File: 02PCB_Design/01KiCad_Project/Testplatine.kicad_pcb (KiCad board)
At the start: 2 copper layers, 42.1 x 42.1 mm, 10 parts, among them J2 MTSW-104-22-L-D-265-RA, U1 ISM330BXTR, U2 AS5047P-ATSM

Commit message: Layout progress
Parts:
- added C10: 10uF, Capacitor_SMD:C_1210_3225Metric_Pad1.33x2.70mm_HandSolder, F.Cu at (66.4, 105.6)
- added C11: 10uF, Capacitor_SMD:C_1210_3225Metric_Pad1.33x2.70mm_HandSolder, F.Cu at (61.4, 105.6)
- added C12: 10uF, Capacitor_SMD:C_1210_3225Metric_Pad1.33x2.70mm_HandSolder, F.Cu at (56.4, 105.6)
- added C13: 10uF, Capacitor_SMD:C_1210_3225Metric_Pad1.33x2.70mm_HandSolder, F.Cu at (51.4, 105.6)
- added C14: 4.7uF, Capacitor_SMD:C_0805_2012Metric_Pad1.18x1.45mm_HandSolder, F.Cu at (70.6, 105.6)
- added C15: 4.7uF, Capacitor_SMD:C_0805_2012Metric_Pad1.18x1.45mm_HandSolder, F.Cu at (35.7, 133.6)
- added C16: 4.7uF, Capacitor_SMD:C_0805_2012Metric_Pad1.18x1.45mm_HandSolder, F.Cu at (31.1, 129.2)
- added C17: 33nF, Capacitor_SMD:C_0603_1608Metric_Pad1.08x0.95mm_HandSolder, F.Cu at (92.0, 110.0)
- added C18: 2.2uF, Capacitor_SMD:C_0805_2012Metric_Pad1.18x1.45mm_HandSolder, F.Cu at (81.3, 160.3)
- added C19: 0.1uF, Capacitor_SMD:C_0603_1608Metric_Pad1.08x0.95mm_HandSolder, F.Cu at (81.4, 162.2)
- added C20: 220nF, Capacitor_SMD:C_0805_2012Metric_Pad1.18x1.45mm_HandSolder, F.Cu at (90.2, 175.0)
- added C21: 220nF, Capacitor_SMD:C_0805_2012Metric_Pad1.18x1.45mm_HandSolder, F.Cu at (90.2, 172.8)
- added C22: 220nF, Capacitor_SMD:C_0805_2012Metric_Pad1.18x1.45mm_HandSolder, F.Cu at (90.2, 168.4)
- added C23: 1uF, Capacitor_SMD:C_0805_2012Metric_Pad1.18x1.45mm_HandSolder, F.Cu at (90.2, 170.6)
- added C24: 1uF, Capacitor_SMD:C_0805_2012Metric_Pad1.18x1.45mm_HandSolder, F.Cu at (86.3, 172.8)
- added C25: 1uF, Capacitor_SMD:C_0805_2012Metric_Pad1.18x1.45mm_HandSolder, F.Cu at (86.3, 175.0)
- added C26: 47p, Capacitor_SMD:C_0603_1608Metric_Pad1.08x0.95mm_HandSolder, F.Cu at (87.1, 164.3)
- added C27: 47p, Capacitor_SMD:C_0603_1608Metric_Pad1.08x0.95mm_HandSolder, F.Cu at (86.6, 162.7)
- added C28: 0.1uF, Capacitor_SMD:C_0603_1608Metric_Pad1.08x0.95mm_HandSolder, F.Cu at (90.0, 165.4)
- added C29: 0.1uF, Capacitor_SMD:C_0603_1608Metric_Pad1.08x0.95mm_HandSolder, F.Cu at (95.2, 165.4)
- added C30: 0.1uF, Capacitor_SMD:C_0603_1608Metric_Pad1.08x0.95mm_HandSolder, F.Cu at (157.0, 21.7)
- added C31: 33nF, Capacitor_SMD:C_0603_1608Metric_Pad1.08x0.95mm_HandSolder, F.Cu at (157.0, 24.2)
- added C32: 0.1uF, Capacitor_SMD:C_0603_1608Metric_Pad1.08x0.95mm_HandSolder, F.Cu at (157.0, 26.7)
- added C33: 2.2uF, Capacitor_SMD:C_0805_2012Metric_Pad1.18x1.45mm_HandSolder, F.Cu at (81.3, 138.6)
- added C34: 0.1uF, Capacitor_SMD:C_0603_1608Metric_Pad1.08x0.95mm_HandSolder, F.Cu at (81.4, 140.5)
- added C35: 220nF, Capacitor_SMD:C_0805_2012Metric_Pad1.18x1.45mm_HandSolder, F.Cu at (90.3, 153.3)
- added C36: 220nF, Capacitor_SMD:C_0805_2012Metric_Pad1.18x1.45mm_HandSolder, F.Cu at (90.3, 151.1)
- added C37: 220nF, Capacitor_SMD:C_0805_2012Metric_Pad1.18x1.45mm_HandSolder, F.Cu at (90.3, 148.9)
- added C38: 1uF, Capacitor_SMD:C_0805_2012Metric_Pad1.18x1.45mm_HandSolder, F.Cu at (90.3, 146.7)
- added C39: 1uF, Capacitor_SMD:C_0805_2012Metric_Pad1.18x1.45mm_HandSolder, F.Cu at (86.3, 153.3)
- added C4: 100nF, Capacitor_SMD:C_0603_1608Metric_Pad1.08x0.95mm_HandSolder, F.Cu at (97.8, 39.8)
- added C40: 1uF, Capacitor_SMD:C_0805_2012Metric_Pad1.18x1.45mm_HandSolder, F.Cu at (86.3, 151.1)
- added C41: 47p, Capacitor_SMD:C_0603_1608Metric_Pad1.08x0.95mm_HandSolder, F.Cu at (87.1, 142.6)
- added C42: 47p, Capacitor_SMD:C_0603_1608Metric_Pad1.08x0.95mm_HandSolder, F.Cu at (86.6, 141.0)
- added C43: 0.1uF, Capacitor_SMD:C_0603_1608Metric_Pad1.08x0.95mm_HandSolder, F.Cu at (90.0, 143.7)
- added C44: 0.1uF, Capacitor_SMD:C_0603_1608Metric_Pad1.08x0.95mm_HandSolder, F.Cu at (95.2, 143.7)
- added C45: 0.1uF, Capacitor_SMD:C_0603_1608Metric_Pad1.08x0.95mm_HandSolder, F.Cu at (180.1, 21.2)
- added C46: 33nF, Capacitor_SMD:C_0603_1608Metric_Pad1.08x0.95mm_HandSolder, F.Cu at (180.1, 23.7)
- added C47: 0.1uF, Capacitor_SMD:C_0603_1608Metric_Pad1.08x0.95mm_HandSolder, F.Cu at (180.1, 26.2)
- added C48: 2.2uF, Capacitor_SMD:C_0805_2012Metric_Pad1.18x1.45mm_HandSolder, F.Cu at (81.3, 117.3)
- added C49: 0.1uF, Capacitor_SMD:C_0603_1608Metric_Pad1.08x0.95mm_HandSolder, F.Cu at (81.4, 119.2)
- added C5: 10uF, Capacitor_SMD:C_1210_3225Metric_Pad1.33x2.70mm_HandSolder, F.Cu at (98.0, 30.6)
- added C50: 220nF, Capacitor_SMD:C_0805_2012Metric_Pad1.18x1.45mm_HandSolder, F.Cu at (90.3, 132.1)
- added C51: 220nF, Capacitor_SMD:C_0805_2012Metric_Pad1.18x1.45mm_HandSolder, F.Cu at (90.3, 129.9)
- added C52: 220nF, Capacitor_SMD:C_0805_2012Metric_Pad1.18x1.45mm_HandSolder, F.Cu at (90.3, 127.7)
- added C53: 1uF, Capacitor_SMD:C_0805_2012Metric_Pad1.18x1.45mm_HandSolder, F.Cu at (90.3, 125.5)
- added C54: 1uF, Capacitor_SMD:C_0805_2012Metric_Pad1.18x1.45mm_HandSolder, F.Cu at (86.3, 132.1)
- added C55: 1uF, Capacitor_SMD:C_0805_2012Metric_Pad1.18x1.45mm_HandSolder, F.Cu at (86.3, 129.9)
- added C56: 47p, Capacitor_SMD:C_0603_1608Metric_Pad1.08x0.95mm_HandSolder, F.Cu at (87.1, 121.4)
- added C57: 47p, Capacitor_SMD:C_0603_1608Metric_Pad1.08x0.95mm_HandSolder, F.Cu at (86.6, 119.8)
- added C58: 0.1uF, Capacitor_SMD:C_0603_1608Metric_Pad1.08x0.95mm_HandSolder, F.Cu at (90.0, 122.5)
- added C59: 0.1uF, Capacitor_SMD:C_0603_1608Metric_Pad1.08x0.95mm_HandSolder, F.Cu at (95.2, 122.5)
- added C6: 1uF, Capacitor_SMD:C_0603_1608Metric_Pad1.08x0.95mm_HandSolder, F.Cu at (100.6, 35.6)
- added C60: 0.1uF, Capacitor_SMD:C_0603_1608Metric_Pad1.08x0.95mm_HandSolder, F.Cu at (202.0, 20.3)
- added C61: 33nF, Capacitor_SMD:C_0603_1608Metric_Pad1.08x0.95mm_HandSolder, F.Cu at (202.0, 22.8)
- added C62: 0.1uF, Capacitor_SMD:C_0603_1608Metric_Pad1.08x0.95mm_HandSolder, F.Cu at (202.0, 25.3)
- added C63: 2.2nF, Capacitor_SMD:C_0603_1608Metric_Pad1.08x0.95mm_HandSolder, F.Cu at (111.6, 158.2)
- added C64: 2.2nF, Capacitor_SMD:C_0603_1608Metric_Pad1.08x0.95mm_HandSolder, F.Cu at (98.4, 97.5)
- added C65: 2.2nF, Capacitor_SMD:C_0603_1608Metric_Pad1.08x0.95mm_HandSolder, F.Cu at (102.7, 97.5)
- added C66: 2.2nF, Capacitor_SMD:C_0603_1608Metric_Pad1.08x0.95mm_HandSolder, F.Cu at (112.9, 97.5)
- added C67: 2.2nF, Capacitor_SMD:C_0603_1608Metric_Pad1.08x0.95mm_HandSolder, F.Cu at (108.6, 97.5)
- added C68: 2.2nF, Capacitor_SMD:C_0603_1608Metric_Pad1.08x0.95mm_HandSolder, F.Cu at (130.4, 148.6)
- added C69: 2.2nF, Capacitor_SMD:C_0603_1608Metric_Pad1.08x0.95mm_HandSolder, F.Cu at (126.6, 148.6)
- added C7: 47uF, Capacitor_THT:CP_Radial_D8.0mm_P3.50mm, F.Cu at (99.2, 48.9)
- added C70: 0.1uF, Capacitor_SMD:C_0603_1608Metric_Pad1.08x0.95mm_HandSolder, F.Cu at (147.0, 167.5)
- added C71: 0.1uF, Capacitor_SMD:C_0603_1608Metric_Pad1.08x0.95mm_HandSolder, F.Cu at (153.2, 171.1)
- added C8: 470uF, Capacitor_THT:CP_Radial_D16.0mm_P7.50mm, F.Cu at (79.5, 95.0)
- added C9: 470uF, Capacitor_THT:CP_Radial_D16.0mm_P7.50mm, F.Cu at (41.9, 94.7)
- added J1: MTSW-104-22-L-D-265-RA, Connector_PinHeader_2.54mm:PinHeader_2x04_P2.54mm_Horizontal, F.Cu at (271.8, 15.2)
- added J3: FCR7350R, Connector:Banana_Jack_1Pin, F.Cu at (61.0, 95.7)
- added J4: FCR7350R, Connector:Banana_Jack_1Pin, F.Cu at (30.4, 95.7)
- added J5: DE9_Receptacle_MountingHoles, Connector_Dsub:DSUB-9_Female_Horizontal_P2.77x2.84mm_EdgePinOffset4.94mm_Housed_MountingHolesOffset7.48mm, F.Cu at (151.6, 179.4)
- added J6: MTSW-104-22-L-D-265-RA, Connector_PinHeader_2.54mm:PinHeader_2x04_P2.54mm_Horizontal, F.Cu at (106.8, 179.3)
- added J7: Conn_01x06_Pin, Connector_PinHeader_2.54mm:PinHeader_2x03_P2.54mm_Horizontal, F.Cu at (121.5, 179.3)
- added L1: 22uH, Inductor_SMD:L_Wuerth_MAPI-4020, F.Cu at (97.8, 43.0)
- added R1: 100k, Resistor_SMD:R_0603_1608Metric_Pad0.98x0.95mm_HandSolder, F.Cu at (271.6, 31.4)
- added R10: 20, Resistor_SMD:R_0603_1608Metric_Pad0.98x0.95mm_HandSolder, F.Cu at (87.4, 160.1)
- added R11: 20, Resistor_SMD:R_0603_1608Metric_Pad0.98x0.95mm_HandSolder, F.Cu at (85.7, 160.1)
- added R12: 3R, Resistor_SMD:R_0603_1608Metric_Pad0.98x0.95mm_HandSolder, F.Cu at (92.6, 166.4)
- added R13: 3.3m, Resistor_SMD:R_2512_6332Metric_Pad1.40x3.35mm_HandSolder, F.Cu at (75.7, 169.9)
- added R14: 100k, Resistor_SMD:R_0603_1608Metric_Pad0.98x0.95mm_HandSolder, F.Cu at (161.3, 26.7)
- added R15: 4.22k, Resistor_SMD:R_0603_1608Metric_Pad0.98x0.95mm_HandSolder, F.Cu at (161.3, 29.2)
- added R16: 3R, Resistor_SMD:R_0603_1608Metric_Pad0.98x0.95mm_HandSolder, F.Cu at (84.1, 141.4)
- added R17: 20, Resistor_SMD:R_0603_1608Metric_Pad0.98x0.95mm_HandSolder, F.Cu at (87.4, 138.4)
- added R18: 20, Resistor_SMD:R_0603_1608Metric_Pad0.98x0.95mm_HandSolder, F.Cu at (85.7, 138.4)
- added R19: 3R, Resistor_SMD:R_0603_1608Metric_Pad0.98x0.95mm_HandSolder, F.Cu at (92.6, 144.7)
- added R2: 33R, Resistor_SMD:R_0603_1608Metric_Pad0.98x0.95mm_HandSolder, F.Cu at (271.6, 34.0)
- added R20: 3.3m, Resistor_SMD:R_2512_6332Metric_Pad1.40x3.35mm_HandSolder, F.Cu at (75.4, 148.1)
- added R21: 100k, Resistor_SMD:R_0603_1608Metric_Pad0.98x0.95mm_HandSolder, F.Cu at (184.5, 26.2)
- added R22: 4.22k, Resistor_SMD:R_0603_1608Metric_Pad0.98x0.95mm_HandSolder, F.Cu at (184.5, 28.7)
- added R23: 3R, Resistor_SMD:R_0603_1608Metric_Pad0.98x0.95mm_HandSolder, F.Cu at (84.1, 120.2)
- added R24: 20, Resistor_SMD:R_0603_1608Metric_Pad0.98x0.95mm_HandSolder, F.Cu at (87.4, 117.2)
- added R25: 20, Resistor_SMD:R_0603_1608Metric_Pad0.98x0.95mm_HandSolder, F.Cu at (85.7, 117.2)
- added R26: 3R, Resistor_SMD:R_0603_1608Metric_Pad0.98x0.95mm_HandSolder, F.Cu at (92.6, 123.4)
- added R27: 3.3m, Resistor_SMD:R_2512_6332Metric_Pad1.40x3.35mm_HandSolder, F.Cu at (75.2, 127.3)
- added R28: 100k, Resistor_SMD:R_0603_1608Metric_Pad0.98x0.95mm_HandSolder, F.Cu at (206.3, 25.3)
- added R29: 4.22k, Resistor_SMD:R_0603_1608Metric_Pad0.98x0.95mm_HandSolder, F.Cu at (206.3, 27.9)
- added R3: 100k, Resistor_SMD:R_0603_1608Metric_Pad0.98x0.95mm_HandSolder, F.Cu at (271.6, 36.5)
- added R30: 33R, Resistor_SMD:R_0603_1608Metric_Pad0.98x0.95mm_HandSolder, F.Cu at (108.8, 159.2)
- added R31: 20R, Resistor_SMD:R_0603_1608Metric_Pad0.98x0.95mm_HandSolder, F.Cu at (112.4, 161.0)
- added R32: 33R, Resistor_SMD:R_0603_1608Metric_Pad0.98x0.95mm_HandSolder, F.Cu at (114.2, 159.2)
- added R33: 20R, Resistor_SMD:R_0603_1608Metric_Pad0.98x0.95mm_HandSolder, F.Cu at (112.1, 100.1)
- added R34: 20R, Resistor_SMD:R_0603_1608Metric_Pad0.98x0.95mm_HandSolder, F.Cu at (109.6, 100.3)
- added R35: 20R, Resistor_SMD:R_0603_1608Metric_Pad0.98x0.95mm_HandSolder, F.Cu at (99.4, 100.1)
- added R36: 20R, Resistor_SMD:R_0603_1608Metric_Pad0.98x0.95mm_HandSolder, F.Cu at (101.7, 100.1)
- added R37: 20R, Resistor_SMD:R_0603_1608Metric_Pad0.98x0.95mm_HandSolder, F.Cu at (129.4, 145.8)
- added R38: 20R, Resistor_SMD:R_0603_1608Metric_Pad0.98x0.95mm_HandSolder, F.Cu at (127.3, 145.8)
- added R39: 33R, Resistor_SMD:R_0603_1608Metric_Pad0.98x0.95mm_HandSolder, B.Cu at (142.2, 157.8)
- added R4: 33R, Resistor_SMD:R_0603_1608Metric_Pad0.98x0.95mm_HandSolder, F.Cu at (271.6, 39.0)
- added R40: 33R, Resistor_SMD:R_0603_1608Metric_Pad0.98x0.95mm_HandSolder, B.Cu at (120.8, 158.0)
- added R41: 33R, Resistor_SMD:R_0603_1608Metric_Pad0.98x0.95mm_HandSolder, B.Cu at (125.8, 158.0)
- added R42: 0R, Resistor_SMD:R_0603_1608Metric_Pad0.98x0.95mm_HandSolder, F.Cu at (151.8, 161.3)
- added R45: 0R, Resistor_SMD:R_0603_1608Metric_Pad0.98x0.95mm_HandSolder, F.Cu at (149.8, 161.3)
- added R46: 120, Resistor_SMD:R_0603_1608Metric_Pad0.98x0.95mm_HandSolder, F.Cu at (148.1, 175.0)
- added R7: 100k, Resistor_SMD:R_0603_1608Metric_Pad0.98x0.95mm_HandSolder, F.Cu at (90.4, 106.6)
- added R8: 4.22k, Resistor_SMD:R_0603_1608Metric_Pad0.98x0.95mm_HandSolder, F.Cu at (90.4, 110.0)
- added R9: 3R, Resistor_SMD:R_0603_1608Metric_Pad0.98x0.95mm_HandSolder, F.Cu at (84.1, 163.1)
- added U10: INA240A1PW, Package_SO:TSSOP-8_4.4x3mm_P0.65mm, F.Cu at (74.8, 121.2)
- added U11: NUCLEO-G431RB, footprints:NucleoMorphoG431RB, F.Cu at (124.5, 121.7)
- added U12: MCP2562FD, Package_SO:SOIC-8_3.9x4.9mm_P1.27mm, F.Cu at (148.6, 171.1)
- added U3: L6982, Package_SO:TSSOP-8_3x3mm_P0.65mm, F.Cu at (98.0, 35.6)
- added U4: AP2114D, Package_TO_SOT_SMD:TO-252-2, F.Cu at (35.8, 126.2)
- added U5: LMG2100R044RARR, footprints:RAR0016B-MFG, F.Cu at (85.0, 168.4)
- added U6: INA240A1PW, Package_SO:TSSOP-8_4.4x3mm_P0.65mm, F.Cu at (75.6, 163.8)
- added U7: LMG2100R044RARR, footprints:RAR0016B-MFG, F.Cu at (85.0, 146.8)
- added U8: INA240A1PW, Package_SO:TSSOP-8_4.4x3mm_P0.65mm, F.Cu at (75.0, 142.0)
- added U9: LMG2100R044RARR, footprints:RAR0016B-MFG, F.Cu at (85.1, 125.6)
- C1: footprint Capacitor_SMD:C_0402_1005Metric_Pad0.74x0.62mm_HandSolder -> Package_SO:SOIC-8_3.9x4.9mm_P1.27mm
- C2, C3: footprint Capacitor_SMD:C_0402_1005Metric_Pad0.74x0.62mm_HandSolder -> Capacitor_SMD:C_0603_1608Metric_Pad1.08x0.95mm_HandSolder
- J2: value MTSW-104-22-L-D-265-RA -> Screw_Terminal_01x03; footprint MyFootprintLib:SAMTEC_MTSW-104-22-L-D-265-RA -> TerminalBlock_Phoenix:TerminalBlock_Phoenix_MKDS-3-3-5.08_1x03_P5.08mm_Horizontal
- U1: value ISM330BXTR -> AS5047P-ATSM; footprint MyFootprintLib:XDCR_ISM330BXTR -> Package_SO:TSSOP-14_4.4x5mm_P0.65mm
- U2: value AS5047P-ATSM -> ISM330BXTR; footprint MyFootprintLib:SOP65P640X120-14N -> Package_LGA:LGA-14_3x2.5mm_P0.5mm_LayoutBorder3x4y; moved to F.Cu
- moved H4 200.1 mm to (275.0, 144.9)
- moved H1 187.6 mm to (275.0, 130.0)
- moved H2 182.7 mm to (275.0, 140.2)
- moved C3 182.7 mm to (271.6, 28.9), turned to 0 degrees
- moved H3 179.1 mm to (275.0, 150.3)
- moved U1 176.9 mm to (278.2, 28.5), turned to 0 degrees
- moved U2 174.8 mm to (271.8, 42.3), turned to 0 degrees
- moved C1 174.1 mm to (278.0, 35.1), turned to 0 degrees
- moved C2 168.2 mm to (271.6, 26.4)
- moved J2 101.4 mm to (26.5, 143.3), turned to -90 degrees
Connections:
- C1 pad 1: /SensorSheet/3.3SPI -> +3.3VP
- C1 pad 2: GND -> GND1
- C2 pad 1: /SensorSheet/3.3SPI -> +3.3VP
- C2 pad 2: GND -> GND1
- C3 pad 1: /SensorSheet/3.3SPI -> +3.3VP
- C3 pad 2: GND -> GND1
- U1 pad 1: /SensorSheet/SPI_MISO -> /SensorSheet/ENC_CS
- U1 pad 11: /SensorSheet/3.3SPI -> +3.3VP
- U1 pad 12: /SensorSheet/IMU_CS -> +3.3VP
- U1 pad 13: /SensorSheet/SPI_SCLK -> GND1
- U1 pad 14: /SensorSheet/SPI_MOSI -> unconnected-(U1-I/PWM-Pad14)
- U1 pad 2: /SensorSheet/3.3SPI -> /SensorSheet/SPI_SCLK
- U1 pad 3: /SensorSheet/3.3SPI -> Net-(U1-MISO)
- U1 pad 4: /SensorSheet/IMU_INT1 -> /SensorSheet/SPI_MOSI
- U1 pad 5: /SensorSheet/3.3SPI -> GND1
- U1 pad 6: /SensorSheet/3.3SPI -> unconnected-(U1-B-Pad6)
- U1 pad 7: GND -> unconnected-(U1-A-Pad7)
- U1 pad 8: /SensorSheet/3.3SPI -> unconnected-(U1-W/PWM-Pad8)
- U1 pad 9: /SensorSheet/3.3SPI -> unconnected-(U1-V-Pad9)
- U2 pad 1: /SensorSheet/ENC_CS -> Net-(U2-SDO/TA0)
- U2 pad 11: /SensorSheet/3.3SPI -> +3.3VP
- U2 pad 12: /SensorSheet/3.3SPI -> /SensorSheet/IMU_CS
- U2 pad 13: GND -> /SensorSheet/SPI_SCLK
- U2 pad 14: unconnected-(U2-I/PWM-Pad14) -> /SensorSheet/SPI_MOSI
- U2 pad 2: /SensorSheet/SPI_SCLK -> +3.3VP
- U2 pad 3: /SensorSheet/SPI_MISO -> +3.3VP
- U2 pad 4: /SensorSheet/SPI_MOSI -> /SensorSheet/IMU_INT1
- U2 pad 5: GND -> +3.3VP
- U2 pad 6: unconnected-(U2-B-Pad6) -> +3.3VP
- U2 pad 7: unconnected-(U2-A-Pad7) -> GND1
- U2 pad 8: unconnected-(U2-W/PWM-Pad8) -> +3.3VP
- U2 pad 9: unconnected-(U2-V-Pad9) -> +3.3VP
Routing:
- net /SensorSheet/3.3SPI: track 77.4 -> 0.00 mm, vias 1 -> 0
- net /SensorSheet/SPI_MOSI: track 24.8 -> 0.00 mm, vias 1 -> 0
- net /SensorSheet/IMU_INT1: track 23.3 -> 0.00 mm
- net /SensorSheet/SPI_MISO: track 19.6 -> 0.00 mm, vias 1 -> 0
- net /SensorSheet/SPI_SCLK: track 19.1 -> 0.00 mm, vias 1 -> 0
- net /SensorSheet/ENC_CS: track 15.6 -> 0.00 mm
- net /SensorSheet/IMU_CS: track 14.9 -> 0.00 mm
- net GND: track 4.01 -> 0.00 mm, vias 4 -> 0
- added copper zone on F.Cu, net +24V
- added copper zone on F.Cu, net GNDPWR
- removed copper zone on B.Cu, net GND
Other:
- board size 42.1 x 42.1 mm -> 146 x 100 mm
- copper layers 2 -> 4
- board text removed: "locked"

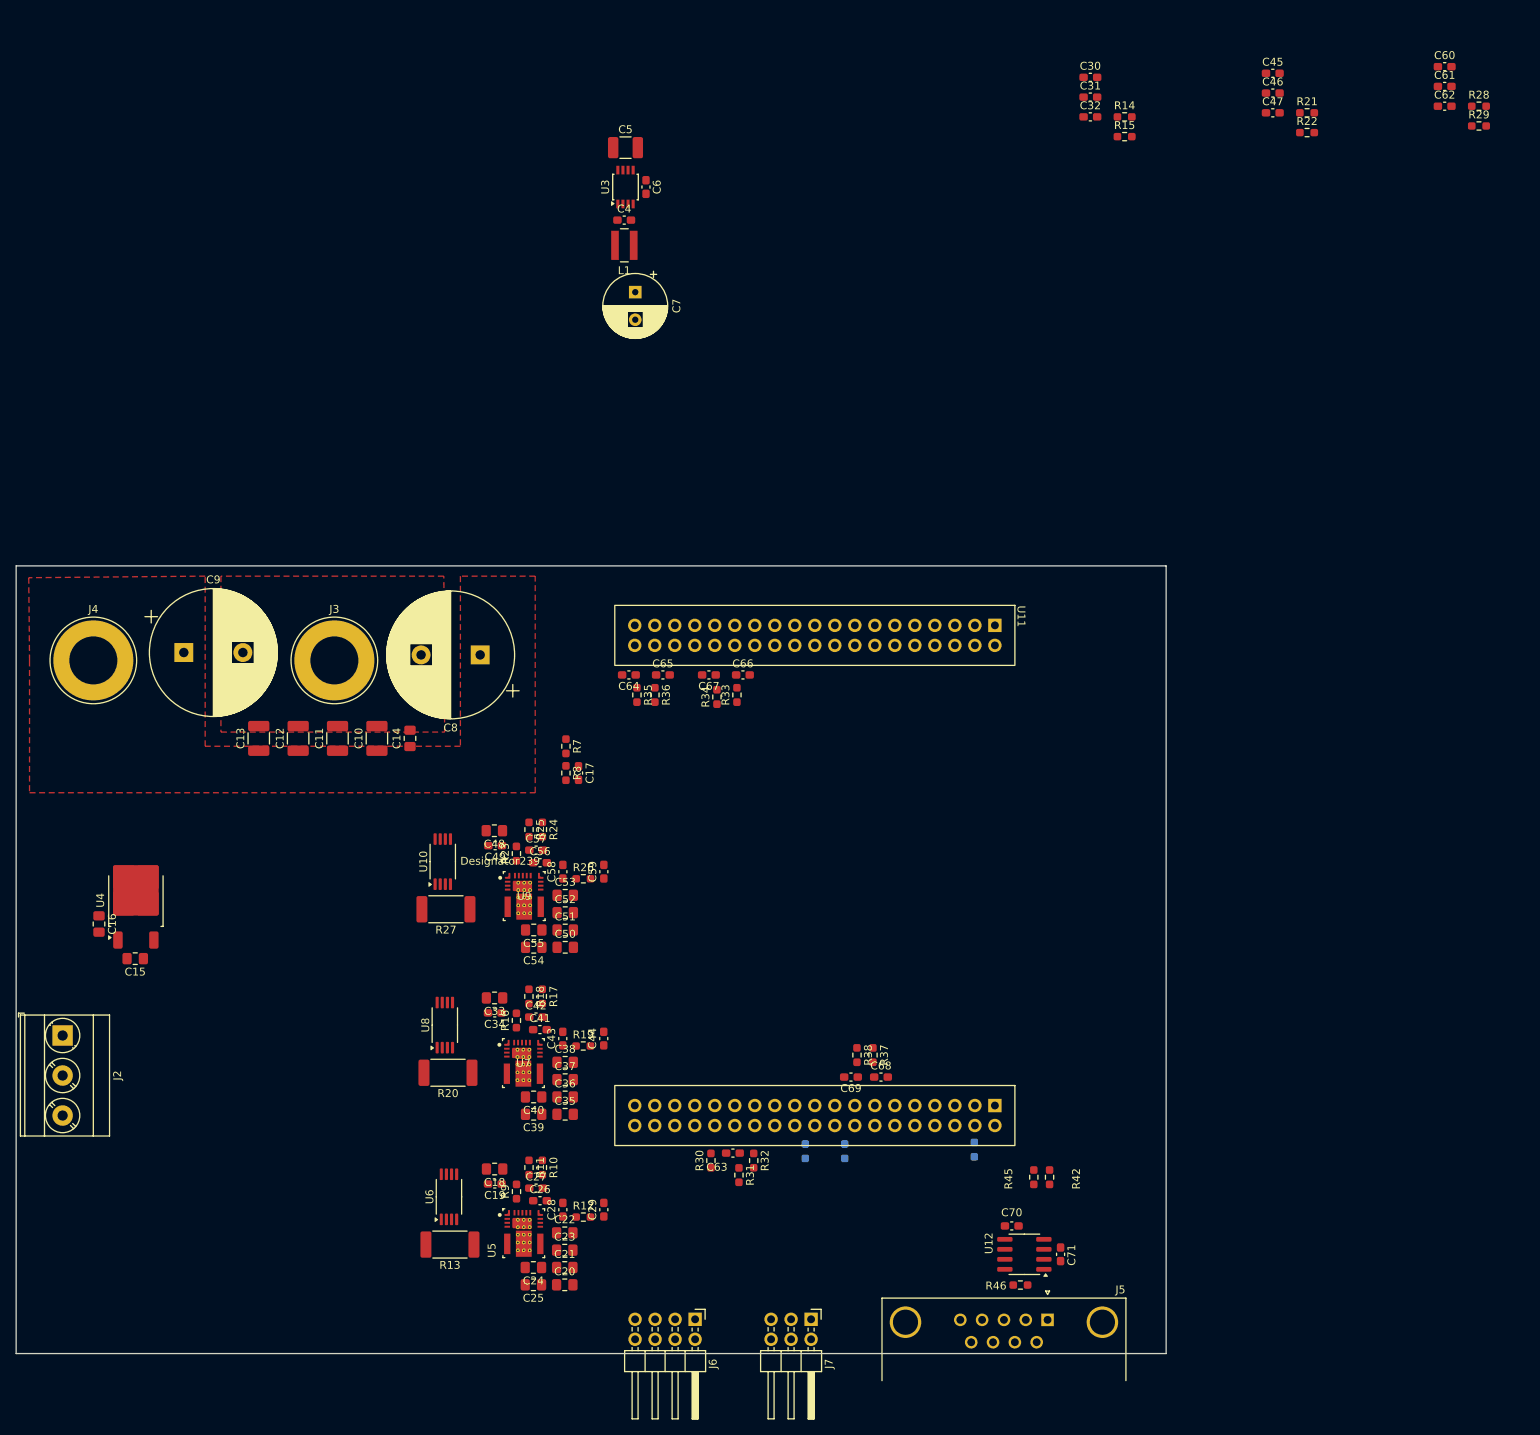
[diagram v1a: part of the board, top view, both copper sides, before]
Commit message: routed signals
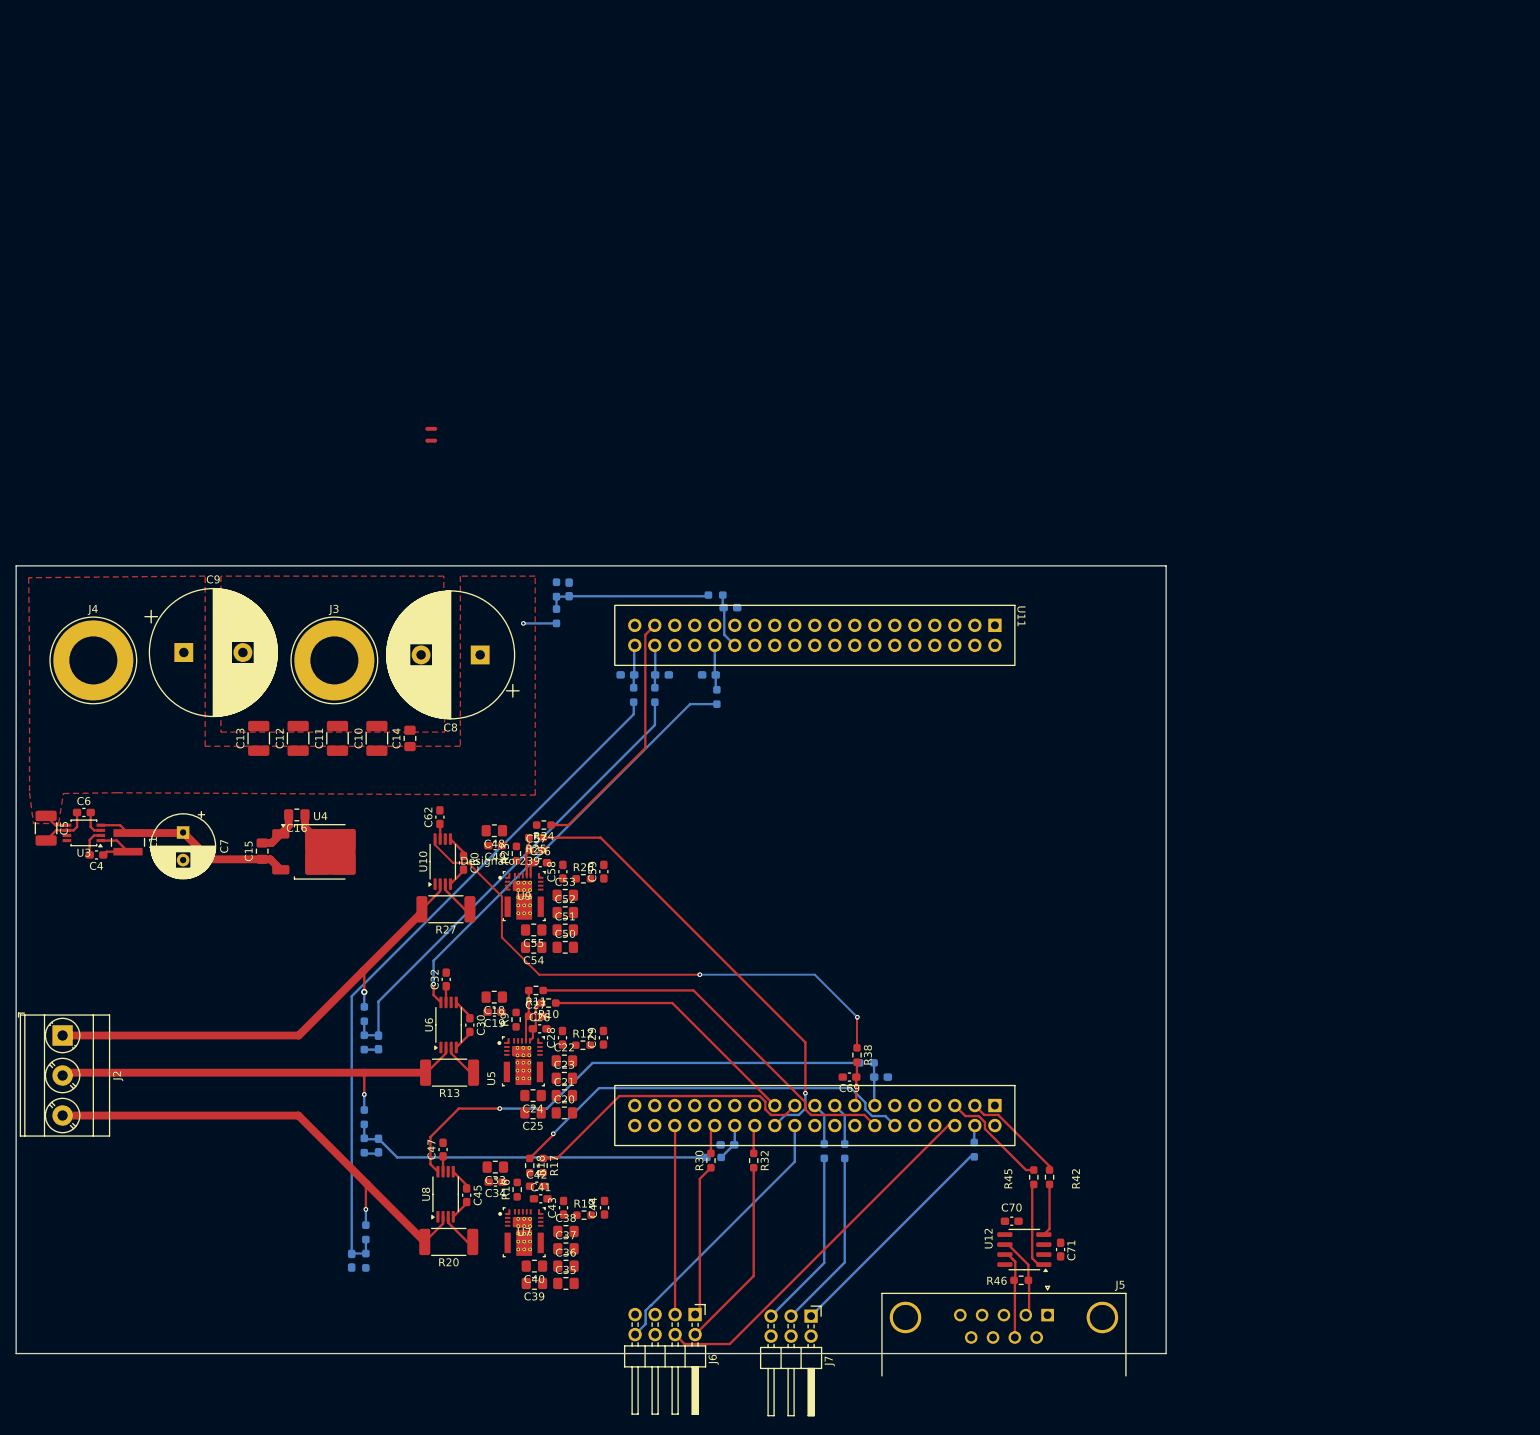
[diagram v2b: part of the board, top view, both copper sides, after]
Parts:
- added NT1: NetTie_2, NetTie:NetTie-2_SMD_Pad0.5mm, F.Cu at (73.3, 66.3)
- added NT2: NetTie_2, NetTie:NetTie-2_SMD_Pad0.5mm, F.Cu at (73.3, 67.8)
- C17, C31, C46, C61, C63, C64, C65, C66, C67, C68, R14, R15, R21, R22, R28, R29, R31, R33, R34, R35, R36, R37, R7, R8: moved to B.Cu
- moved C46 188.8 mm to (63.2, 171.9), turned to -90 degrees
- moved R22 186.5 mm to (65.0, 171.9), turned to -90 degrees
- moved R21 185.7 mm to (65.0, 168.3), turned to -90 degrees
- moved R29 183.2 mm to (64.8, 144.2), turned to -90 degrees
- moved R28 182.5 mm to (64.8, 140.6), turned to -90 degrees
- moved C61 181.8 mm to (66.6, 144.2), turned to -90 degrees
- moved C45 175.4 mm to (77.8, 163.6), turned to -90 degrees
- moved C47 168.6 mm to (74.8, 157.8), turned to 90 degrees
- moved C31 160.9 mm to (66.6, 157.3), turned to -90 degrees
- moved C60 160.4 mm to (77.4, 121.4), turned to -90 degrees
- moved R15 160.4 mm to (64.8, 157.3), turned to -90 degrees
- moved R14 159.5 mm to (64.8, 153.7), turned to -90 degrees
- moved C62 156.3 mm to (74.4, 115.6), turned to 90 degrees
- moved C30 143.8 mm to (78.2, 142.0), turned to -90 degrees
- moved C32 136.7 mm to (75.2, 136.2), turned to 90 degrees
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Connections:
- J2 pad 2: /escSheet/HalfBridgePowerStage2/PH_OUT -> /escSheet/HalfBridgePowerStage1/PH_OUT
- J2 pad 3: /escSheet/HalfBridgePowerStage1/PH_OUT -> /escSheet/HalfBridgePowerStage2/PH_OUT
- J5 pad 9: unconnected-(J5-Pad9) -> +5V
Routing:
- net /escSheet/HalfBridgePowerStage2/V_PHASE: track 0.00 -> 88.4 mm
- net /escSheet/HalfBridgePowerStage3/I_PHASE: track 0.00 -> 70.4 mm, vias 0 -> 2
- net /escSheet/HalfBridgePowerStage2/I_PHASE: track 0.00 -> 63.2 mm, vias 0 -> 1
- net /escSheet/HalfBridgePowerStage2/PH_OUT: track 0.00 -> 62.1 mm, vias 0 -> 1
- net /escSheet/HalfBridgePowerStage3/PH_OUT: track 0.00 -> 60.9 mm, vias 0 -> 1
- net /escSheet/HalfBridgePowerStage3/V_PHASE: track 0.00 -> 60.4 mm
- net /escSheet/HalfBridgePowerStage3/PWM_LI: track 0.00 -> 57.2 mm, vias 0 -> 1
- net /escSheet/HalfBridgePowerStage1/I_PHASE: track 0.00 -> 55.1 mm, vias 0 -> 1
- net /escSheet/HalfBridgePowerStage1/PH_OUT: track 0.00 -> 54.7 mm, vias 0 -> 1
- net /escSheet/HalfBridgePowerStage2/PWM_LI: track 0.00 -> 52.6 mm, vias 0 -> 1
- net /escSheet/HalfBridgePowerStage1/PWM_LI: track 0.00 -> 49.7 mm
- net /escSheet/Bus_Connectors/IMU_CS: track 0.00 -> 47.5 mm
- net /escSheet/HalfBridgePowerStage1/V_PHASE: track 0.00 -> 46.2 mm
- net /escSheet/HalfBridgePowerStage2/PWM_HI: track 0.00 -> 37.1 mm
- net /escSheet/Bus_Connectors/IMU_INT1: track 0.00 -> 35.0 mm
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
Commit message: Design 1.0 Finished
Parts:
- removed NT1, NT2: NetTie_2, NetTie:NetTie-2_SMD_Pad0.5mm
- C1: footprint Package_SO:SOIC-8_3.9x4.9mm_P1.27mm -> Capacitor_SMD:C_0603_1608Metric_Pad1.08x0.95mm_HandSolder; moved to B.Cu
- R1, R2, U1: moved to B.Cu
- moved J1 88.0 mm to (220.3, 86.6), turned to 135 degrees
- moved U1 79.6 mm to (233.2, 94.1), turned to -135 degrees
- moved C1 78.7 mm to (229.2, 96.9), turned to 135 degrees
- moved C5 74.7 mm to (83.0, 70.7), turned to 180 degrees
- moved H4 74.4 mm to (220.7, 94.1)
- moved R2 71.6 mm to (229.1, 91.5), turned to -45 degrees
- moved R1 71.2 mm to (229.2, 88.7), turned to -45 degrees
- moved C2 68.6 mm to (241.6, 88.2), turned to 90 degrees
- moved C6 68.4 mm to (85.0, 75.5), turned to 90 degrees
- moved U3 67.9 mm to (82.5, 75.5), turned to 90 degrees
- moved C4 65.3 mm to (79.7, 77.1), turned to 90 degrees
- moved C3 64.4 mm to (240.6, 85.4)
- moved R3 64.0 mm to (234.4, 88.5), turned to 180 degrees
- moved H1 63.9 mm to (233.2, 81.6)
- moved H3 63.3 mm to (245.7, 94.1)
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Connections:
- C10 pad 2: GNDPWR -> GNDA
- C11 pad 2: GNDPWR -> GNDA
- C12 pad 2: GNDPWR -> GNDA
- C13 pad 2: GNDPWR -> GNDA
- C14 pad 2: GNDPWR -> GNDA
- C20 pad 2: GNDPWR -> GNDA
- C21 pad 2: GNDPWR -> GNDA
- C22 pad 2: GNDPWR -> GNDA
- C23 pad 2: GNDPWR -> GNDA
- C24 pad 2: GNDPWR -> GNDA
- C25 pad 2: GNDPWR -> GNDA
- C35 pad 2: GNDPWR -> GNDA
- C36 pad 2: GNDPWR -> GNDA
- C37 pad 2: GNDPWR -> GNDA
- C38 pad 2: GNDPWR -> GNDA
- C39 pad 2: GNDPWR -> GNDA
- C40 pad 2: GNDPWR -> GNDA
- C50 pad 2: GNDPWR -> GNDA
- C51 pad 2: GNDPWR -> GNDA
- C52 pad 2: GNDPWR -> GNDA
- C53 pad 2: GNDPWR -> GNDA
- C54 pad 2: GNDPWR -> GNDA
- C55 pad 2: GNDPWR -> GNDA
- C7 pad 2: GNDPWR -> GNDA
- C8 pad 2: GNDPWR -> GNDA
- C9 pad 2: GNDPWR -> GNDA
- J1 pad 1: (no net) -> /SensorSheet/IMU_INT1
- J1 pad 2: (no net) -> /SensorSheet/SPI_MOSI
- J1 pad 3: (no net) -> /SensorSheet/SPI_MISO
- J1 pad 4: (no net) -> +3.3VP
- J1 pad 5: (no net) -> /SensorSheet/IMU_CS
- J1 pad 6: (no net) -> /SensorSheet/ENC_CS
- J1 pad 7: (no net) -> /SensorSheet/SPI_SCLK
- J1 pad 8: (no net) -> GND1
- J3 pad 1: GNDPWR -> GNDA
- J5 pad 9: +5V -> +3.3V
- U11 pad L_19: GNDPWR -> GNDA
- U11 pad L_20: GNDPWR -> GNDA
- U11 pad L_22: GNDPWR -> GNDA
- U11 pad L_8: GNDPWR -> GNDA
- U11 pad R_20: GNDPWR -> GNDA
- U11 pad R_9: GNDPWR -> GNDA
- U3 pad 8: GNDPWR -> GNDA
- U5 pad 17: GNDPWR -> GNDA
- U5 pad 6: GNDPWR -> GNDA
- U7 pad 17: GNDPWR -> GNDA
- U7 pad 6: GNDPWR -> GNDA
- U9 pad 17: GNDPWR -> GNDA
- U9 pad 6: GNDPWR -> GNDA
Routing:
- net +5V: track 25.2 -> 355.4 mm, vias 0 -> 4
- net +3.3V: track 17.9 -> 320.2 mm, vias 0 -> 9
- net GNDA: track 22.8 -> 115.0 mm, vias 0 -> 147
- net /escSheet/HalfBridgePowerStage2/PH_OUT: track 62.1 -> 9.46 mm
- net /escSheet/HalfBridgePowerStage3/PH_OUT: track 60.9 -> 8.78 mm
- net /escSheet/HalfBridgePowerStage1/PH_OUT: track 54.7 -> 8.96 mm
- net /SensorSheet/SPI_MOSI: track 0.00 -> 25.7 mm, vias 0 -> 1
- net /SensorSheet/SPI_MISO: track 0.00 -> 25.7 mm
- net /SensorSheet/IMU_INT1: track 0.00 -> 24.6 mm
- net /escSheet/Bus_Connectors/SPI_MISO: track 0.00 -> 24.6 mm
- net +3.3VP: track 0.00 -> 19.4 mm, vias 0 -> 5
- net /SensorSheet/SPI_SCLK: track 0.00 -> 18.0 mm, vias 0 -> 1
- net /SensorSheet/ENC_CS: track 0.00 -> 17.9 mm
- net /SensorSheet/IMU_CS: track 0.00 -> 17.3 mm
- net +24V: track 7.34 -> 19.5 mm, vias 1 -> 61
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- added copper zone on In2.Cu, net +24V
- added copper zone on In2.Cu, net +3.3VP
- added copper zone on F.Cu, net /escSheet/HalfBridgePowerStage1/PH_OUT
- added copper zone on F.Cu, net /escSheet/HalfBridgePowerStage1/SW
- added copper zone on F.Cu, net /escSheet/HalfBridgePowerStage2/PH_OUT
- added copper zone on F.Cu, net /escSheet/HalfBridgePowerStage2/SW
- added copper zone on F.Cu, net /escSheet/HalfBridgePowerStage3/PH_OUT
- added copper zone on F.Cu, net /escSheet/HalfBridgePowerStage3/SW
- added copper zone on In1.Cu, net GND1
- added copper zone on F.Cu, net GNDA
- added copper zone on In1.Cu, net GNDA
- removed copper zone on F.Cu, net GNDPWR
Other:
- board size 146 x 100 mm -> 210.4 x 100 mm
- board text added: "Azmi Beyrouti azmi.beyrouti@diehl.com"
- board text added: "GND ENC_CS 3.3V MOSI"
- board text added: "SCLK IMU_CS MISO IMU_INT"
- board text added: "⌀25mm M4"
